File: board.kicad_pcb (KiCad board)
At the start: 2 copper layers, 77.1 x 37.1 mm, 34 parts, among them J0 Battery Pads, J1 AVR-ISP-6, J2 Micro_SD_Card_Det, J3 USB_B_Micro, SW0 RESET, SW1 POWER, SW2 UP, SW3 DOWN, SW4 LEFT, SW5 RIGHT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

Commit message: Updated Layout
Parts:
- J0, LS1: moved to B.Cu
- SW1: value POWER -> UP; footprint Buttons_Switches_SMD:SW_DIP_x1_W8.61mm_Slide_LowProfile -> Buttons_Switches_SMD:SW_SPST_PTS645
- SW2: value UP -> DOWN
- SW3: value DOWN -> LEFT
- SW4: value LEFT -> RIGHT
- SW5: value RIGHT -> BTN_A
- SW6: value BTN_A -> BTN_B
- SW7: value BTN_B -> BTN_C
- SW8: value BTN_C -> POWER; footprint Buttons_Switches_SMD:SW_SPST_PTS645 -> Buttons_Switches_SMD:SW_DIP_x1_W8.61mm_Slide_LowProfile
- U1: footprint Pin_Headers:Pin_Header_Straight_1x07_Pitch1.27mm -> Custom Footprints:128x128_OLED
- moved SW3 54.3 mm to (113.8, 105.5), turned to 90 degrees
- moved R0 52.9 mm to (122.0, 89.2), turned to 180 degrees
- moved J0 47.9 mm to (112.2, 112.0), turned to 90 degrees
- moved R2 45.7 mm to (134.3, 109.0)
- moved J3 45.5 mm to (176.2, 84.8)
- moved U2 44.2 mm to (164.0, 86.7), turned to 90 degrees
- moved U3 41.4 mm to (138.2, 91.2), turned to 90 degrees
- moved C4 40.5 mm to (145.8, 108.5)
- moved J1 39.7 mm to (132.0, 75.0)
- moved SW2 36.1 mm to (121.5, 111.8), turned to 270 degrees
- moved C2 34.7 mm to (141.5, 89.2), turned to 90 degrees
- moved SW7 34.4 mm to (187.3, 116.0), turned to 180 degrees
- moved LS1 34.1 mm to (174.7, 95.5)
- moved SW8 32.1 mm to (126.2, 85.5), turned to 180 degrees
- moved J2 30.8 mm to (153.8, 111.0)
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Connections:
- J2 pad 1: Net-(J2-Pad1) -> GND
- J2 pad 10: Net-(J2-Pad10) -> SD_DETECT
- J2 pad 2: Net-(J2-Pad2) -> SD_CS
- J2 pad 3: Net-(J2-Pad3) -> SD_MOSI
- J2 pad 5: Net-(J2-Pad5) -> SD_SCK
- J2 pad 7: Net-(J2-Pad7) -> SD_MISO
- J2 pad 8: Net-(J2-Pad8) -> GND
- J2 pad 9: Net-(J2-Pad9) -> +3V3
- SW1 pad 1: Net-(C2-Pad1) -> +3V3
- SW1 pad 2: +BATT -> UP
- SW2 pad 2: UP -> DOWN
- SW3 pad 2: DOWN -> LEFT
- SW4 pad 2: LEFT -> RIGHT
- SW5 pad 2: RIGHT -> BTN_A
- SW6 pad 2: BTN_A -> BTN_B
- SW7 pad 2: BTN_B -> BTN_C
- SW8 pad 1: +3V3 -> Net-(C2-Pad1)
- SW8 pad 2: BTN_C -> +BATT
- U0 pad 19: Net-(U0-Pad19) -> SD_SCK
- U0 pad 20: Net-(U0-Pad20) -> SD_MOSI
- U0 pad 21: Net-(U0-Pad21) -> SD_MISO
- U0 pad 22: Net-(U0-Pad22) -> SD_CS
- U0 pad 23: Net-(U0-Pad23) -> SD_DETECT
- U0 pad 31: BTN_C -> BTN_A
- U0 pad 33: BTN_A -> BTN_C
- U0 pad 40: D_SCK -> D_CS
- U0 pad 41: D_MOSI -> D_DC
- U0 pad 43: D_CS -> D_MOSI
- U0 pad 44: D_DC -> D_SCK
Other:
- board size 77.1 x 37.1 mm -> 96.3 x 46.3 mm

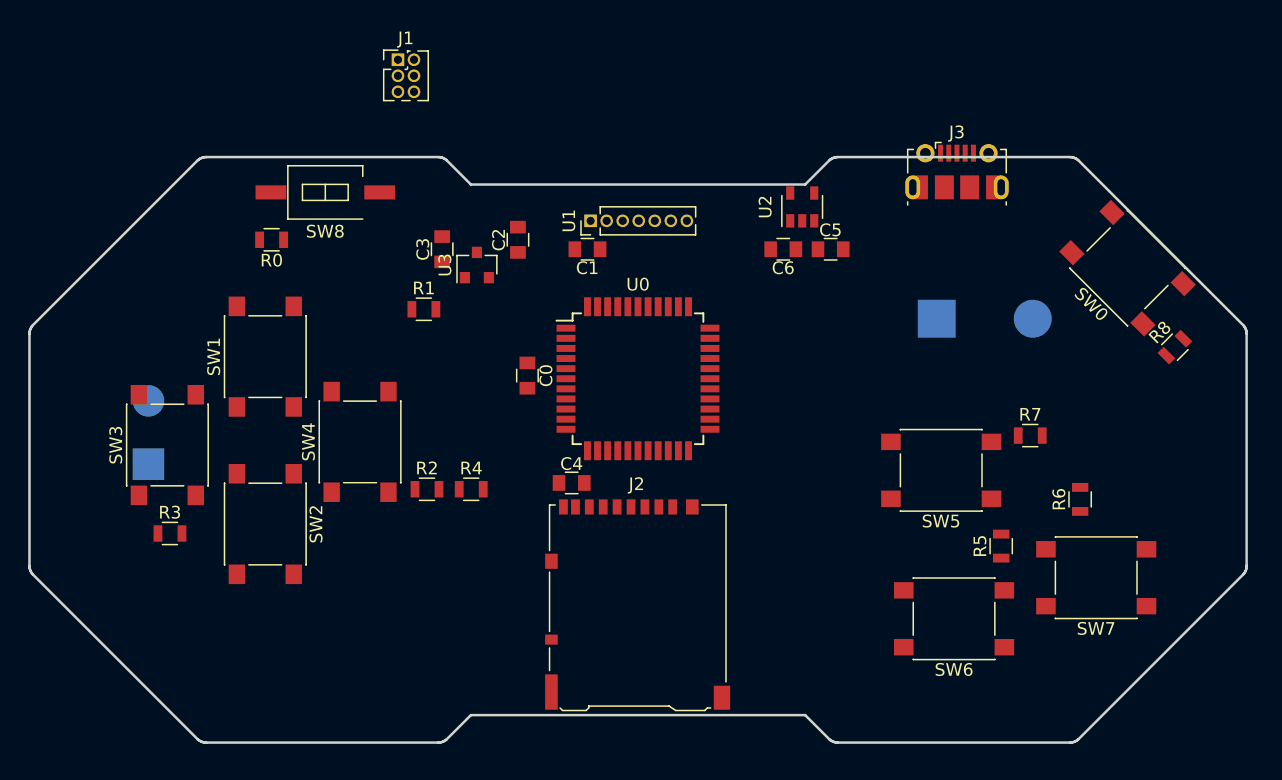
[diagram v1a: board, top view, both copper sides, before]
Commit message: Added tracks
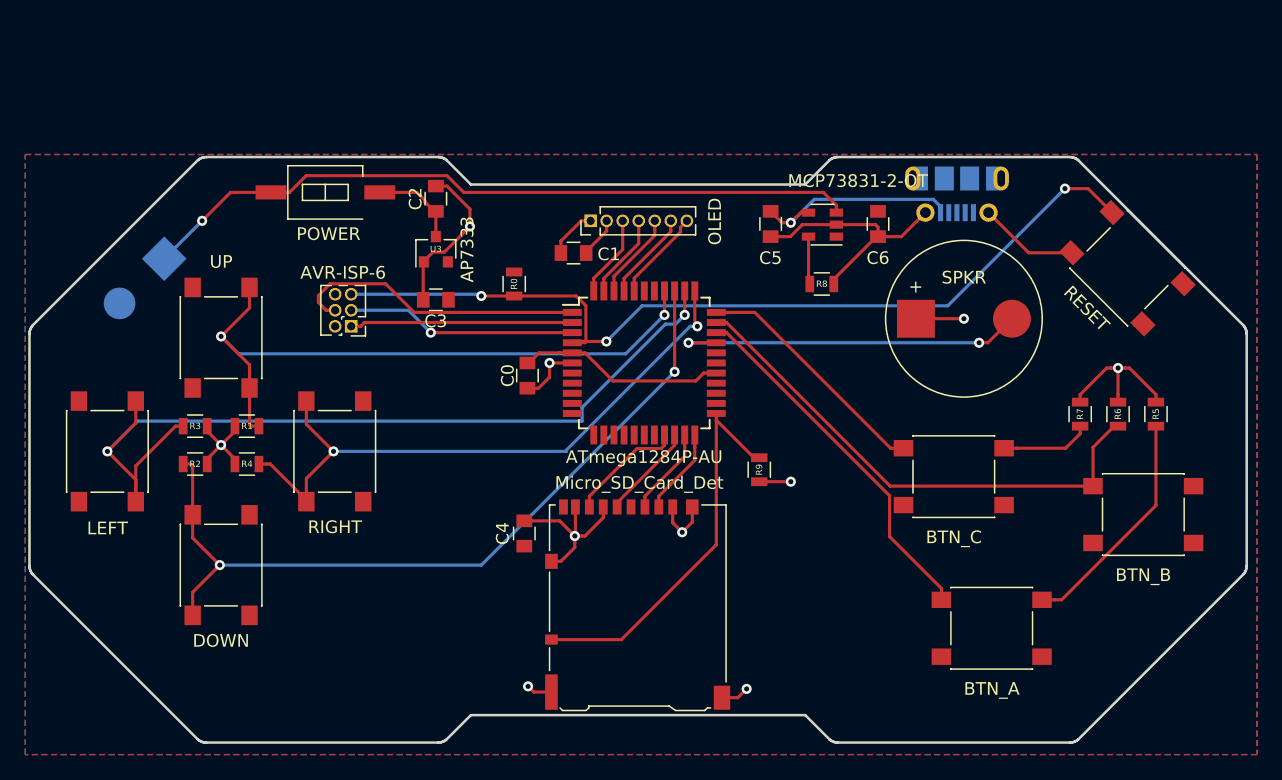
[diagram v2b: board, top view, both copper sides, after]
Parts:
- added R9: 1K, Resistors_SMD:R_0805, F.Cu at (160.6, 107.5)
- J3: moved to B.Cu
- LS1: moved to F.Cu
- moved R8 28.4 mm to (165.6, 92.8), turned to 0 degrees
- moved J0 25.2 mm to (117.0, 87.2), turned to 225 degrees
- moved J1 21.4 mm to (128.3, 96.1), turned to 180 degrees
- moved R0 19.5 mm to (141.2, 92.8), turned to 270 degrees
- moved R2 18.5 mm to (116.0, 107.0)
- moved R4 17.9 mm to (120.0, 107.0), turned to 180 degrees
- moved SW6 17.1 mm to (191.0, 111.0)
- moved R1 16.8 mm to (120.0, 104.0), turned to 180 degrees
- moved R5 16.1 mm to (192.0, 103.0)
- moved SW7 13.8 mm to (176.0, 108.0)
- moved SW5 13.1 mm to (179.0, 120.0)
- moved R3 8.73 mm to (116.0, 104.0)
- moved C6 7.76 mm to (170.0, 88.0), turned to 270 degrees
- moved R6 7.39 mm to (189.0, 103.0)
- moved C2 7.27 mm to (135.0, 86.0)
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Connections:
- U0 pad 19: SD_SCK -> SD_MISO
- U0 pad 20: SD_MOSI -> SD_SCK
- U0 pad 21: SD_MISO -> SD_MOSI
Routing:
- net GND: track 0.00 -> 97.5 mm, vias 0 -> 10
- net RESET: track 0.00 -> 71.5 mm, vias 0 -> 3
- net LEFT: track 0.00 -> 70.5 mm, vias 0 -> 2
- net DOWN: track 0.00 -> 63.2 mm, vias 0 -> 2
- net +BATT: track 0.00 -> 57.5 mm, vias 0 -> 1
- net UP: track 0.00 -> 52.3 mm, vias 0 -> 2
- net RIGHT: track 0.00 -> 50.6 mm, vias 0 -> 2
- net BTN_A: track 0.00 -> 47.4 mm
- net BTN_B: track 0.00 -> 40.9 mm
- net SD_DETECT: track 0.00 -> 31.2 mm
- net SND: track 0.00 -> 28.6 mm, vias 0 -> 2
- net BTN_C: track 0.00 -> 26.4 mm
- net MOSI: track 0.00 -> 23.6 mm
- net +3V3: track 0.00 -> 19.7 mm
- net SCK: track 0.00 -> 18.2 mm, vias 0 -> 1
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- added copper zone on F.Cu, net +3V3
- added copper zone on B.Cu, net GND

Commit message: tweak
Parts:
- J1: value AVR-ISP-6 -> PGRM
- J2: value Micro_SD_Card_Det -> Micro SD Slot
- SW5: value BTN_A -> A
- SW6: value BTN_B -> B
- SW7: value BTN_C -> C
- U0: value ATmega1284P-AU -> ATmega1284P
- U2: value MCP73831-2-OT -> Chg Ctrl
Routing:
- net +3V3: track 19.7 -> 36.6 mm
- net +BATT: track 57.5 -> 60.8 mm
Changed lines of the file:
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@@
     (thickness 1.6)
     (drawings 100)
-    (tracks 292)
+    (tracks 300)
     (zones 0)
     (modules 35)
@@
     (43 Eco2.User user hide)
     (44 Edge.Cuts user)
-    (45 Margin user)
-    (46 B.CrtYd user)
-    (47 F.CrtYd user)
+    (45 Margin user hide)
+    (46 B.CrtYd user hide)
+    (47 F.CrtYd user hide)
     (48 B.Fab user hide)
-    (49 F.Fab user)
+    (49 F.Fab user hide)
   )
   (setup
@@
   (module "Custom Footprints:LiPo_Pads" (layer B.Cu)
     (at 117.035534 87.214466 225)
-    (fp_text reference J0 (at 7.5 -2.5 225) (layer B.SilkS)
+    (fp_text reference J0 (at 7.5 -2.5 225) (layer B.Fab)
       (effects (font (size 1 1) (thickness 0.15)) (justify mirror))
     )
@@
       (effects (font (size 1 1) (thickness 0.15)))
     )
-    (fp_text value AVR-ISP-6 (at 0.635 4.235 180) (layer F.SilkS)
+    (fp_text value PGRM (at 0.635 4.235 180) (layer F.SilkS)
       (effects (font (size 1 1) (thickness 0.15)))
     )
@@
       (effects (font (size 1 1) (thickness 0.15)))
     )
-    (fp_text value Micro_SD_Card_Det (at -2.65 -2.5) (layer F.SilkS)
+    (fp_text value "Micro SD Slot" (at -2.65 -2.5) (layer F.SilkS)
       (effects (font (size 1 1) (thickness 0.15)))
     )
@@
     (tags "Micro-USB SMD Typ-B")
     (attr smd)
-    (fp_text reference J3 (at 0 4) (layer B.SilkS)
+    (fp_text reference J3 (at 0 4) (layer B.Fab)
       (effects (font (size 1 1) (thickness 0.15)) (justify mirror))
     )
@@
       (effects (font (size 1 1) (thickness 0.15)))
     )
-    (fp_text value BTN_A (at 0 -4.8 180) (layer F.SilkS)
+    (fp_text value A (at 0 -4.8 180) (layer F.SilkS)
       (effects (font (size 1 1) (thickness 0.15)))
     )
@@
       (effects (font (size 1 1) (thickness 0.15)))
     )
-    (fp_text value BTN_B (at 0 -4.8 180) (layer F.SilkS)
+    (fp_text value B (at 0 -4.8 180) (layer F.SilkS)
       (effects (font (size 1 1) (thickness 0.15)))
     )
@@
       (effects (font (size 1 1) (thickness 0.15)))
     )
-    (fp_text value BTN_C (at 0 -4.8 180) (layer F.SilkS)
+    (fp_text value C (at 0 -4.8 180) (layer F.SilkS)
       (effects (font (size 1 1) (thickness 0.15)))
     )
@@
       (effects (font (size 1 1) (thickness 0.15)))
     )
-    (fp_text value ATmega1284P-AU (at 0 7.45) (layer F.SilkS)
+    (fp_text value ATmega1284P (at 0 7.45) (layer F.SilkS)
       (effects (font (size 1 1) (thickness 0.15)))
     )
@@
       (effects (font (size 1 1) (thickness 0.15)))
     )
-    (fp_text value MCP73831-2-OT (at -2.8 3.45 180) (layer F.SilkS)
+    (fp_text value "Chg Ctrl" (at -2.8 3.45 180) (layer F.SilkS)
       (effects (font (size 1 1) (thickness 0.15)))
     )
@@
   (gr_line (start 116.23444 128.858) (end 116.32222 128.915) (layer Edge.Cuts) (width 0.2))
   (gr_line (start 135.5 129) (end 135.59772 128.9625) (layer Edge.Cuts) (width 0.2))
-  (via (at 153.1 95.2) (size 0.8) (drill 0.4) (layers F.Cu B.Cu) (net 25))
-  (via (at 178 97.4) (size 0.8) (drill 0.4) (layers F.Cu B.Cu) (net 24))
-  (via (at 138.6 93.7) (size 0.8) (drill 0.4) (layers F.Cu B.Cu) (net 21))
-  (via (at 134.6 96.6) (size 0.8) (drill 0.4) (layers F.Cu B.Cu) (net 22))
   (segment (start 126.322894 94.83) (end 125.7 94.207106) (width 0.25) (layer F.Cu) (net 1))
   (segment (start 127.03 94.83) (end 126.322894 94.83) (width 0.25) (layer F.Cu) (net 1))
@@
   (segment (start 142.375 99) (end 143.175 98.2) (width 0.25) (layer F.Cu) (net 2))
   (segment (start 142.25 99) (end 142.375 99) (width 0.25) (layer F.Cu) (net 2))
+  (segment (start 151.5 102.9) (end 146.8 98.2) (width 0.25) (layer F.Cu) (net 2))
+  (segment (start 151.5 104.7) (end 151.5 102.9) (width 0.25) (layer F.Cu) (net 2))
   (segment (start 146.8 98.2) (end 145.8 98.2) (width 0.25) (layer F.Cu) (net 2))
-  (segment (start 149.025001 100.425001) (end 146.8 98.2) (width 0.25) (layer F.Cu) (net 2))
-  (segment (start 155.574999 100.425001) (end 149.025001 100.425001) (width 0.25) (layer F.Cu) (net 2))
-  (segment (start 156.2 99.8) (end 155.574999 100.425001) (width 0.25) (layer F.Cu) (net 2))
+  (segment (start 156.2 99.8) (end 155 101) (width 0.25) (layer F.Cu) (net 2))
   (segment (start 157.2 99.8) (end 156.2 99.8) (width 0.25) (layer F.Cu) (net 2))
+  (segment (start 151.5 103.7) (end 151.5 104.7) (width 0.25) (layer F.Cu) (net 2))
+  (segment (start 154.2 101) (end 151.5 103.7) (width 0.25) (layer F.Cu) (net 2))
+  (segment (start 155 101) (end 154.2 101) (width 0.25) (layer F.Cu) (net 2))
+  (segment (start 151.5 95.1) (end 151.5 104.7) (width 0.25) (layer F.Cu) (net 2))
+  (segment (start 152.3 93.3) (end 152.3 94.3) (width 0.25) (layer F.Cu) (net 2))
+  (segment (start 152.3 94.3) (end 151.5 95.1) (width 0.25) (layer F.Cu) (net 2))
   (via (at 146 112.7) (size 0.8) (drill 0.4) (layers F.Cu B.Cu) (net 3))
   (via (at 118 105.5) (size 0.8) (drill 0.4) (layers F.Cu B.Cu) (net 3))
@@
   (segment (start 166.7 86.525) (end 165.675 85.5) (width 0.25) (layer F.Cu) (net 20))
   (segment (start 166.7 87.1) (end 166.7 86.525) (width 0.25) (layer F.Cu) (net 20))
+  (segment (start 166.8 87) (end 166.7 87.1) (width 0.25) (layer F.Cu) (net 20))
+  (segment (start 170 87) (end 166.8 87) (width 0.25) (layer F.Cu) (net 20))
+  (via (at 138.6 93.7) (size 0.8) (drill 0.4) (layers F.Cu B.Cu) (net 21))
   (segment (start 146.8 97.4) (end 145.8 97.4) (width 0.25) (layer F.Cu) (net 21))
   (segment (start 146.875001 97.324999) (end 146.8 97.4) (width 0.25) (layer F.Cu) (net 21))
@@
   (segment (start 145.9 97.3) (end 145.8 97.4) (width 0.25) (layer F.Cu) (net 21))
   (segment (start 148.5 97.3) (end 145.9 97.3) (width 0.25) (layer F.Cu) (net 21))
+  (via (at 134.6 96.6) (size 0.8) (drill 0.4) (layers F.Cu B.Cu) (net 22))
   (segment (start 134.6 96.6) (end 145.8 96.6) (width 0.25) (layer F.Cu) (net 22))
   (segment (start 132.83 94.83) (end 134.6 96.6) (width 0.25) (layer B.Cu) (net 22))
@@
   (segment (start 129.05 96.1) (end 129.35 95.8) (width 0.25) (layer F.Cu) (net 23))
   (segment (start 128.3 96.1) (end 129.05 96.1) (width 0.25) (layer F.Cu) (net 23))
+  (via (at 178 97.4) (size 0.8) (drill 0.4) (layers F.Cu B.Cu) (net 24))
   (via (at 155 97.4) (size 0.8) (drill 0.4) (layers F.Cu B.Cu) (net 24))
   (segment (start 178.7 97.4) (end 178 97.4) (width 0.25) (layer F.Cu) (net 24))
@@
   (segment (start 155 97.4) (end 157.2 97.4) (width 0.25) (layer F.Cu) (net 24))
   (segment (start 178 97.4) (end 155 97.4) (width 0.25) (layer B.Cu) (net 24))
+  (via (at 153.1 95.2) (size 0.8) (drill 0.4) (layers F.Cu B.Cu) (net 25))
   (segment (start 120.4 104) (end 121 104) (width 0.25) (layer F.Cu) (net 25))
   (segment (start 120.25 103.85) (end 120.4 104) (width 0.25) (layer F.Cu) (net 25))

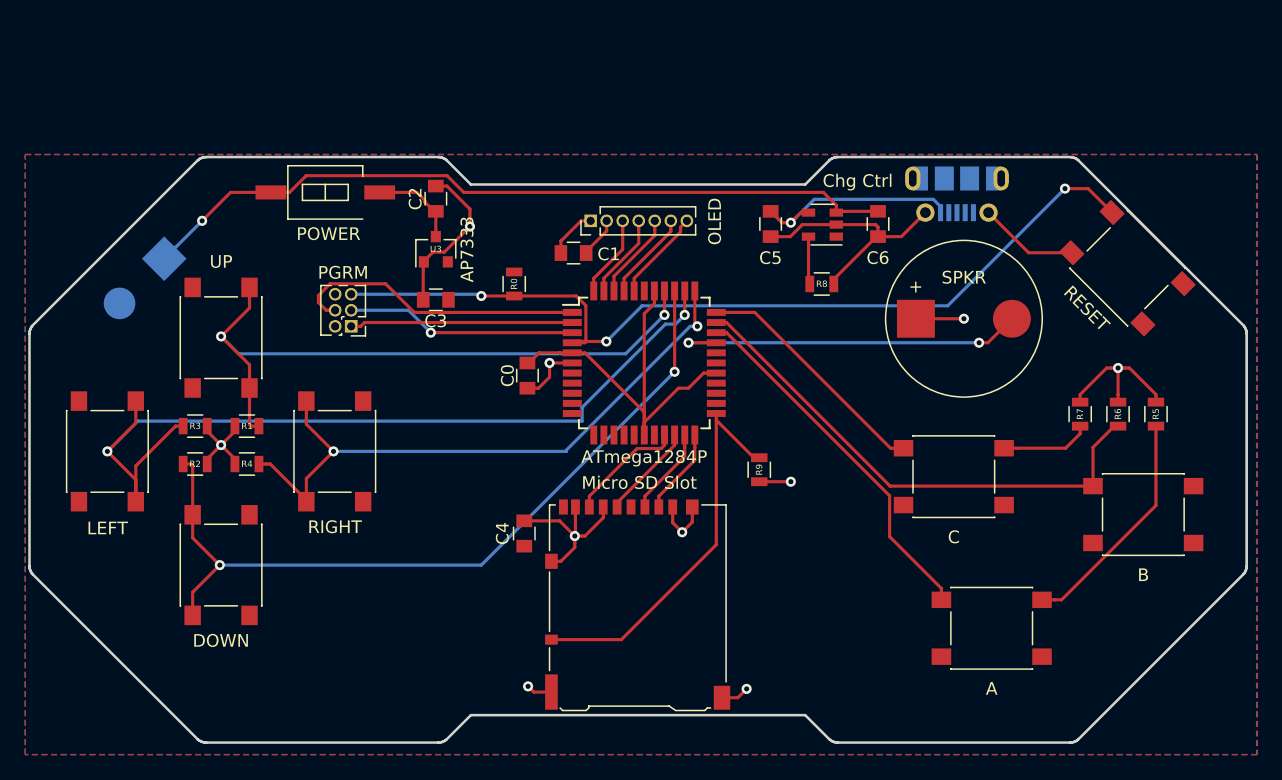
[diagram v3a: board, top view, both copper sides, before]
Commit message: added crystal
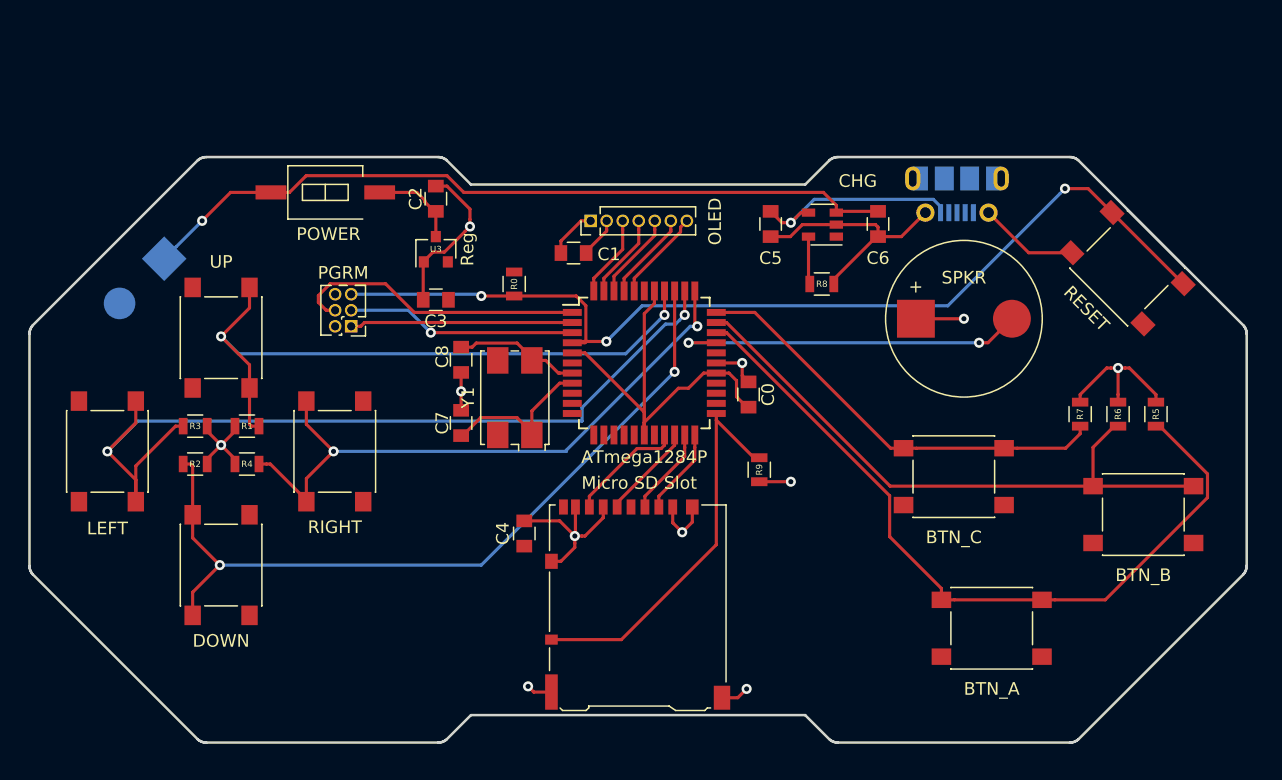
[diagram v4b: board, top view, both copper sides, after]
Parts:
- added C7: 22pF, Capacitors_SMD:C_0805, F.Cu at (137.0, 103.8)
- added C8: 22pF, Capacitors_SMD:C_0805, F.Cu at (137.0, 98.8)
- added Y1: 16MHz, Crystals:Crystal_SMD_7050-4pin_7.0x5.0mm, F.Cu at (141.2, 101.8)
- SW5: value A -> BTN_A
- SW6: value B -> BTN_B
- SW7: value C -> BTN_C
- U2: value Chg Ctrl -> CHG
- U3: value AP7333 -> Reg
- moved C0 17.6 mm to (159.8, 101.5), turned to 90 degrees
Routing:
- net BTN_A: track 47.4 -> 60.9 mm
- net Net-(C7-Pad1): track 0.00 -> 12.9 mm
- net Net-(C8-Pad1): track 0.00 -> 10.0 mm
- net RESET: track 71.5 -> 79.4 mm
- net BTN_C: track 26.4 -> 34.3 mm
- net BTN_B: track 40.9 -> 48.9 mm
- net GND: track 97.5 -> 99.3 mm, vias 10 -> 11
- net +3V3: track 36.6 -> 37.1 mm
- removed copper zone on F.Cu, net +3V3
- removed copper zone on B.Cu, net GND

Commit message: Revert "added crystal"
This reverts commit 60f505991b0e3ccfce5c63fb45a6584053ac2d9c.
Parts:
- removed C7, C8: 22pF, Capacitors_SMD:C_0805
- removed Y1: 16MHz, Crystals:Crystal_SMD_7050-4pin_7.0x5.0mm
- SW5: value BTN_A -> A
- SW6: value BTN_B -> B
- SW7: value BTN_C -> C
- U2: value CHG -> Chg Ctrl
- U3: value Reg -> AP7333
- moved C0 17.6 mm to (142.2, 100.0), turned to 270 degrees
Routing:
- net BTN_A: track 60.9 -> 47.4 mm
- net Net-(U0-Pad8): track 12.9 -> 0.00 mm
- net Net-(U0-Pad7): track 10.0 -> 0.00 mm
- net RESET: track 79.4 -> 71.5 mm
- net BTN_C: track 34.3 -> 26.4 mm
- net BTN_B: track 48.9 -> 40.9 mm
- net GND: track 99.3 -> 97.5 mm, vias 11 -> 10
- net +3V3: track 37.1 -> 36.6 mm
- added copper zone on F.Cu, net +3V3
- added copper zone on B.Cu, net GND
